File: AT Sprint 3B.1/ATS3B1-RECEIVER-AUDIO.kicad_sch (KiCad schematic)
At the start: 55 parts, among them J6 SPK, U1 SA612A, U2 SA612A, U3 LM4808, U4 74LVC1G3157, U5 AN6123MS, Y1 4.9152MHz, Y2 4.9152MHz, Y3 4.9152MHz, Y4 4.9152MHz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

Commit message: fix C11 footprint
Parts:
- CT1: footprint Capacitor_SMD:C_Trimmer_Murata_TZB4-A -> CraftsmanICs:C_TRIMMER_TZ03
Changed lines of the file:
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@@
       (effects (font (size 1.27 1.27)) (justify left))
     )
-    (property "Footprint" "Capacitor_SMD:C_Trimmer_Murata_TZB4-A" (id 2) (at 158.75 48.26 0)
+    (property "Footprint" "CraftsmanICs:C_TRIMMER_TZ03" (id 2) (at 158.75 48.26 0)
       (effects (font (size 1.27 1.27)) hide)
     )

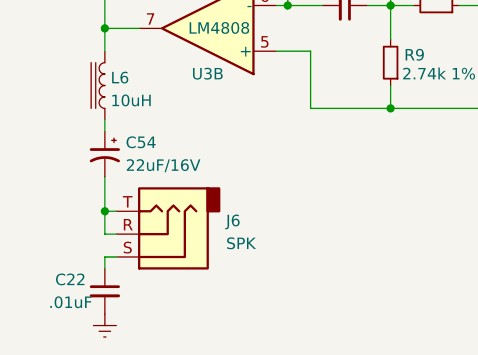
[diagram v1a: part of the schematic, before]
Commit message: fix C22 TRS connection error
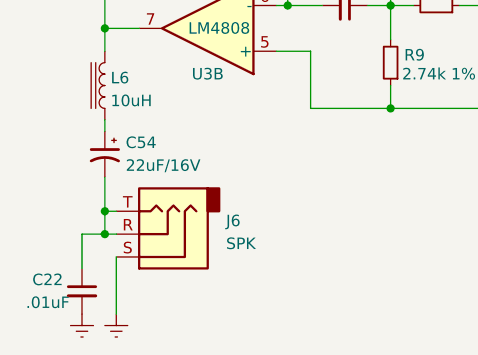
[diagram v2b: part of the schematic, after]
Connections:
- net GNDREF: now also J6.S
- net at C54.2, J6.R, J6.T: now also C22.1
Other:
- moved on the sheet: C22
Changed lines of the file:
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@@
   (junction (at 107.95 30.48) (diameter 0) (color 0 0 0 0)
+  )
+  (junction (at 26.67 104.14) (diameter 0) (color 0 0 0 0)
   )
   (junction (at 26.67 101.6) (diameter 0) (color 0 0 0 0)
@@
     (stroke (width 0) (type default) (color 0 0 0 0))
   )
-  (wire (pts (xy 26.67 107.95) (xy 26.67 106.68))
-    (stroke (width 0) (type default) (color 0 0 0 0))
-  )
   (wire (pts (xy 26.67 97.79) (xy 26.67 101.6))
     (stroke (width 0) (type default) (color 0 0 0 0))
@@
     (stroke (width 0) (type default) (color 0 0 0 0))
   )
-  (wire (pts (xy 26.67 106.68) (xy 27.94 106.68))
-    (stroke (width 0) (type default) (color 0 0 0 0))
-  )
   (wire (pts (xy 85.09 99.06) (xy 88.9 99.06))
     (stroke (width 0) (type default) (color 0 0 0 0))
@@
     (stroke (width 0) (type default) (color 0 0 0 0))
   )
+  (wire (pts (xy 27.94 106.68) (xy 27.94 113.03))
+    (stroke (width 0) (type default) (color 0 0 0 0))
+  )
   (wire (pts (xy 114.3 68.58) (xy 114.3 76.2))
     (stroke (width 0) (type default) (color 0 0 0 0))
@@
     (stroke (width 0) (type default) (color 0 0 0 0))
   )
+  (wire (pts (xy 24.13 104.14) (xy 26.67 104.14))
+    (stroke (width 0) (type default) (color 0 0 0 0))
+  )
   (wire (pts (xy 101.6 57.15) (xy 101.6 67.31))
     (stroke (width 0) (type default) (color 0 0 0 0))
@@
   )
   (wire (pts (xy 40.64 74.93) (xy 46.99 74.93))
+    (stroke (width 0) (type default) (color 0 0 0 0))
+  )
+  (wire (pts (xy 24.13 107.95) (xy 24.13 104.14))
     (stroke (width 0) (type default) (color 0 0 0 0))
   )
@@
     (pin "S")
     (pin "T")
+  )
+  (symbol (lib_id "power:GNDREF") (at 27.94 113.03 0) (unit 1)
+    (in_bom yes) (on_board yes) (fields_autoplaced)
+    (property "Reference" "#PWR?" (id 0) (at 27.94 119.38 0)
+      (effects (font (size 1.27 1.27)) hide)
+    )
+    (property "Value" "GNDREF" (id 1) (at 27.94 117.4734 0)
+      (effects (font (size 1.27 1.27)) hide)
+    )
+    (property "Footprint" "" (id 2) (at 27.94 113.03 0)
+      (effects (font (size 1.27 1.27)) hide)
+    )
+    (property "Datasheet" "" (id 3) (at 27.94 113.03 0)
+      (effects (font (size 1.27 1.27)) hide)
+    )
+    (pin "1")
   )
   (symbol (lib_id "power:GNDREF") (at 153.67 29.21 0) (unit 1)
@@
     (pin "2")
   )
-  (symbol (lib_id "power:GNDREF") (at 26.67 113.03 0) (unit 1)
-    (in_bom yes) (on_board yes) (fields_autoplaced)
-    (property "Reference" "#PWR0165" (id 0) (at 26.67 119.38 0)
-      (effects (font (size 1.27 1.27)) hide)
-    )
-    (property "Value" "GNDREF" (id 1) (at 26.67 117.4734 0)
-      (effects (font (size 1.27 1.27)) hide)
-    )
-    (property "Footprint" "" (id 2) (at 26.67 113.03 0)
-      (effects (font (size 1.27 1.27)) hide)
-    )
-    (property "Datasheet" "" (id 3) (at 26.67 113.03 0)
+  (symbol (lib_id "power:GNDREF") (at 24.13 113.03 0) (unit 1)
+    (in_bom yes) (on_board yes) (fields_autoplaced)
+    (property "Reference" "#PWR0165" (id 0) (at 24.13 119.38 0)
+      (effects (font (size 1.27 1.27)) hide)
+    )
+    (property "Value" "GNDREF" (id 1) (at 24.13 117.4734 0)
+      (effects (font (size 1.27 1.27)) hide)
+    )
+    (property "Footprint" "" (id 2) (at 24.13 113.03 0)
+      (effects (font (size 1.27 1.27)) hide)
+    )
+    (property "Datasheet" "" (id 3) (at 24.13 113.03 0)
       (effects (font (size 1.27 1.27)) hide)
     )
@@
     (pin "2")
   )
-  (symbol (lib_id "Device:C_Small") (at 26.67 110.49 0) (unit 1)
-    (in_bom yes) (on_board yes)
-    (property "Reference" "C22" (id 0) (at 22.86 109.22 0))
-    (property "Value" ".01uF" (id 1) (at 22.86 111.7569 0))
-    (property "Footprint" "Capacitor_SMD:C_0805_2012Metric" (id 2) (at 26.67 110.49 0)
-      (effects (font (size 1.27 1.27)) hide)
-    )
-    (property "Datasheet" "~" (id 3) (at 26.67 110.49 0)
-      (effects (font (size 1.27 1.27)) hide)
-    )
+  (symbol (lib_id "Device:C_Small") (at 24.13 110.49 0) (unit 1)
+    (in_bom yes) (on_board yes)
+    (property "Reference" "C22" (id 0) (at 20.32 109.22 0))
+    (property "Value" ".01uF" (id 1) (at 20.32 111.7569 0))
+    (property "Footprint" "Capacitor_SMD:C_0805_2012Metric" (id 2) (at 24.13 110.49 0)
+      (effects (font (size 1.27 1.27)) hide)
+    )
+    (property "Datasheet" "~" (id 3) (at 24.13 110.49 0)
+      (effects (font (size 1.27 1.27)) hide)
+    )

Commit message: fix some errors. release for pcb production
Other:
- note added: "4 x 4.9152MHz"
- note removed: "4 x 5.9152MHz"
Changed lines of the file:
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@@
     (stroke (width 0) (type default) (color 0 0 0 0))
   )
-  (text "4 x 5.9152MHz" (at 93.98 25.4 0)
+  (text "4 x 4.9152MHz" (at 93.98 25.4 0)
     (effects (font (size 1.27 1.27) (thickness 0.254) bold) (justify left bottom))
   )
@@
   (symbol (lib_id "power:GNDREF") (at 27.94 113.03 0) (unit 1)
     (in_bom yes) (on_board yes) (fields_autoplaced)
-    (property "Reference" "#PWR?" (id 0) (at 27.94 119.38 0)
+    (property "Reference" "#PWR0170" (id 0) (at 27.94 119.38 0)
       (effects (font (size 1.27 1.27)) hide)
     )
